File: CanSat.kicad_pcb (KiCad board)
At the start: 2 copper layers, 55.6 x 55.5 mm, 87 parts, among them IC1 W25Q128JVPIQ, J1 USB_C_Receptacle, J10 Conn_01x04_Pin, J11 Conn_01x03_Socket, J2 Conn_Coaxial, J3 Conn_01x06_Socket, J4 Conn_01x02_Pin, J5 Screw_Terminal_01x02, J6 Conn_01x06_Pin, J7 Conn_01x03_Pin, J8 Conn_01x02_Pin, J9 Conn_01x02_Pin, M2 MountingHole_2.2mm_M2, Q1 BSS138, SW1 SW_Push, SW2 SW_Push, SW3 SW_Push, U1 MPU-6050, U3 Waveshare23721, U4 RFM98W-433S2, U5 RP2350_60QFN, U8 BMP280, U9 APS6404L-3SQR-ZR, Y1 Crystal_GND24

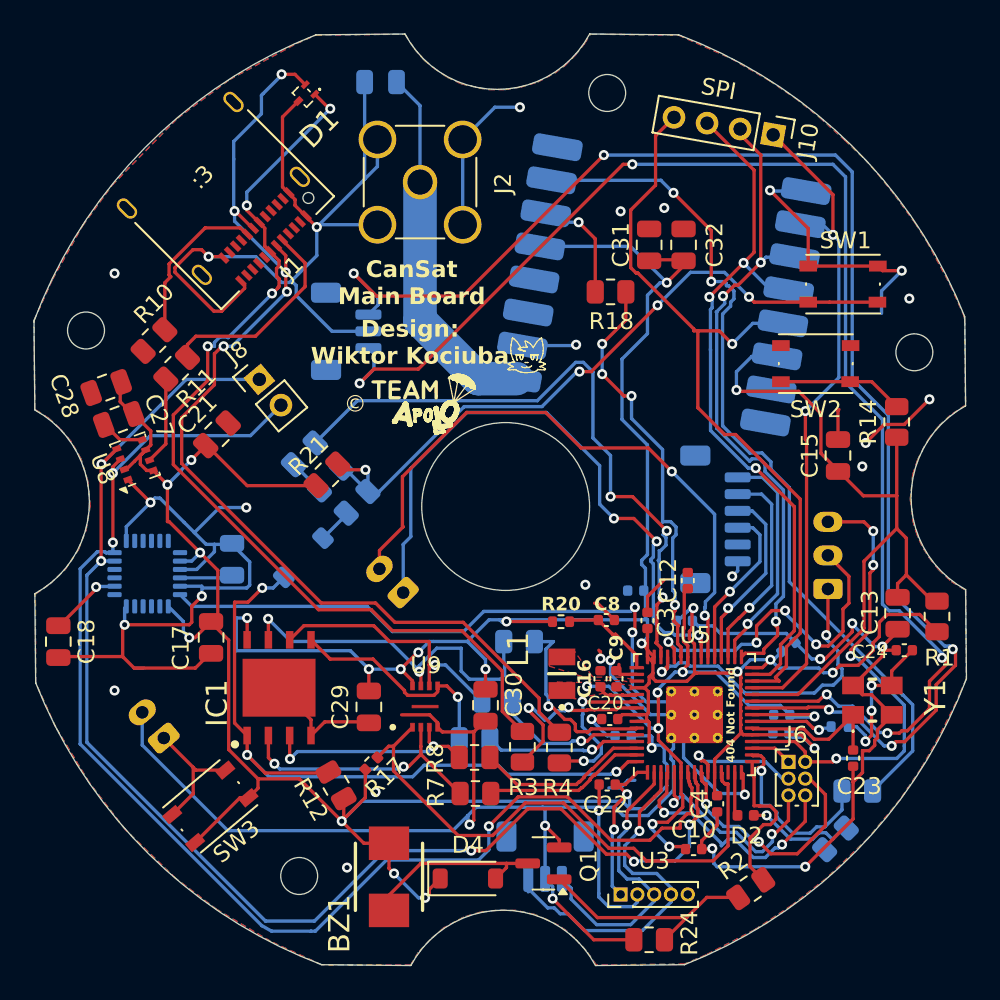
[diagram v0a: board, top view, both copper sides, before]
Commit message: Changed QSPI and added pull-ups on i2c
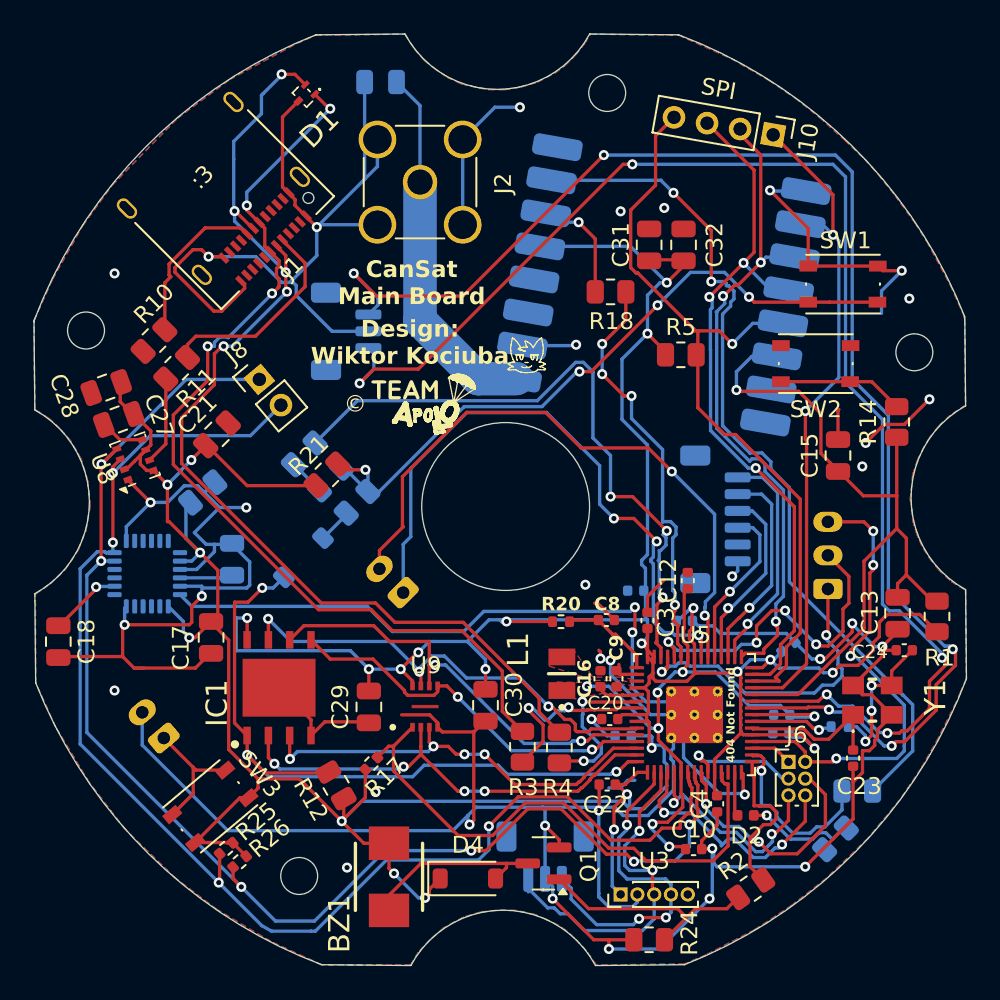
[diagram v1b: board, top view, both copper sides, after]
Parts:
- removed R6, R7, R8, R9: 27, Resistor_SMD:R_0805_2012Metric
- added C25: 10nF, Capacitor_SMD:C_0805_2012Metric, B.Cu at (86.5, 65.2)
- added R25: 4.7K, Resistor_SMD:R_0402_1005Metric, F.Cu at (87.9, 86.3)
- added R26: 4.7K, Resistor_SMD:R_0402_1005Metric, F.Cu at (88.7, 87.2)
- C19: value 2.2nF -> 100nF
- R5: value 27 -> 10K; moved to F.Cu
- Y1: value Crystal_GND24 -> ABM8272T3
- moved R5 23.3 mm to (115.0, 57.0), turned to 0 degrees
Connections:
- R5 pad 1: Net-(U5-QSPI_SCLK) -> +3V3
- R5 pad 2: /QSPI_SCLK -> /SPI0_CSn
- U3 pad 3: /GPS_TX -> /GPS_RX
- U3 pad 4: /GPS_RX -> /GPS_TX
- U5 pad 55: Net-(U5-QSPI_SD3) -> /QSPI_SD3
- U5 pad 56: Net-(U5-QSPI_SCLK) -> /QSPI_SCLK
- U5 pad 57: Net-(U5-QSPI_SD0) -> /QSPI_SD0
- U5 pad 58: Net-(U5-QSPI_SD2) -> /QSPI_SD2
- U5 pad 59: Net-(U5-QSPI_SD1) -> /QSPI_SD1
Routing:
- net GND: track 285.5 -> 298.7 mm, vias 34 -> 36
- net /QSPI_SD2: track 13.3 -> 25.5 mm, vias 2 -> 4
- net Net-(U5-QSPI_SD3): track 11.6 -> 0.00 mm, vias 1 -> 0
- net /QSPI_SD1: track 16.0 -> 27.4 mm, vias 2 -> 4
- net /QSPI_SCLK: track 15.8 -> 26.2 mm, vias 1 -> 2
- net Net-(U5-QSPI_SD2): track 10.3 -> 0.00 mm
- net /QSPI_SD0: track 13.4 -> 23.1 mm, vias 1 -> 2
- net Net-(U5-QSPI_SD1): track 9.68 -> 0.00 mm
- net Net-(U5-QSPI_SD0): track 9.27 -> 0.00 mm, vias 1 -> 0
- net Net-(U5-QSPI_SCLK): track 9.12 -> 0.00 mm, vias 1 -> 0
- net +3V3: track 239.9 -> 248.4 mm, vias 23 -> 24
- net /QSPI_SD3: track 22.0 -> 28.3 mm, vias 2 -> 3
- net /GPS_TX: track 17.4 -> 20.2 mm, vias 1 -> 3
- net /I2C0_SDA: track 80.3 -> 82.1 mm, vias 3 -> 4
- net /I2C0_SCL: track 80.0 -> 81.1 mm, vias 5 -> 6
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
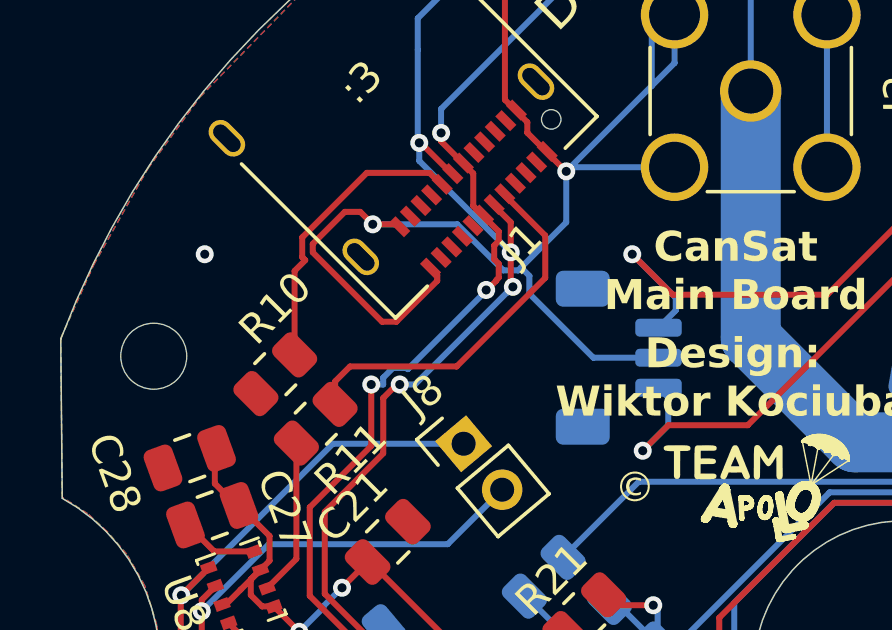
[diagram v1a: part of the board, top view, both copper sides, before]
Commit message: Fixed USB data lines
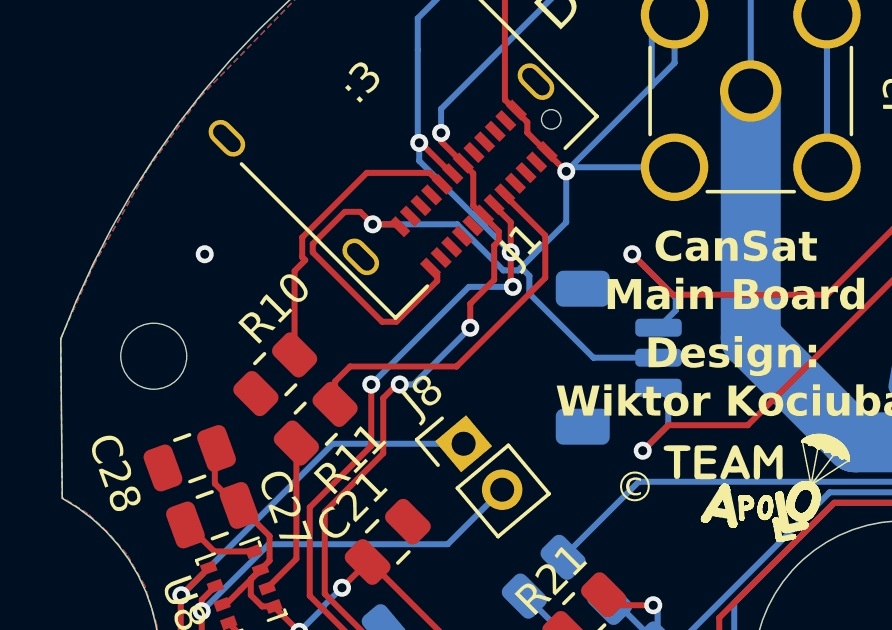
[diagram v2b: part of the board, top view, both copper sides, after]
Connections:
- R3 pad 1: /RP2350A/N_USB_D- -> /RP2350A/N_USB_D+
- R3 pad 2: /USB_D- -> /USB_D+
- R4 pad 1: /USB_D+ -> /USB_D-
- R4 pad 2: /RP2350A/N_USB_D+ -> /RP2350A/N_USB_D-
- U5 pad 51: /RP2350A/N_USB_D+ -> /RP2350A/N_USB_D-
- U5 pad 52: /RP2350A/N_USB_D- -> /RP2350A/N_USB_D+
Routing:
- net /RP2350A/N_USB_D-: track 11.3 -> 9.59 mm
- net /RP2350A/N_USB_D+: track 9.59 -> 11.3 mm
